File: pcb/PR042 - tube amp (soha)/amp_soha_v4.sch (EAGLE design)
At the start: 55 parts, among them IC1 NE5532, IC2 7812, IC3 7912, Q1 J113, Q2 J113, Q3 J113, Q4 J113

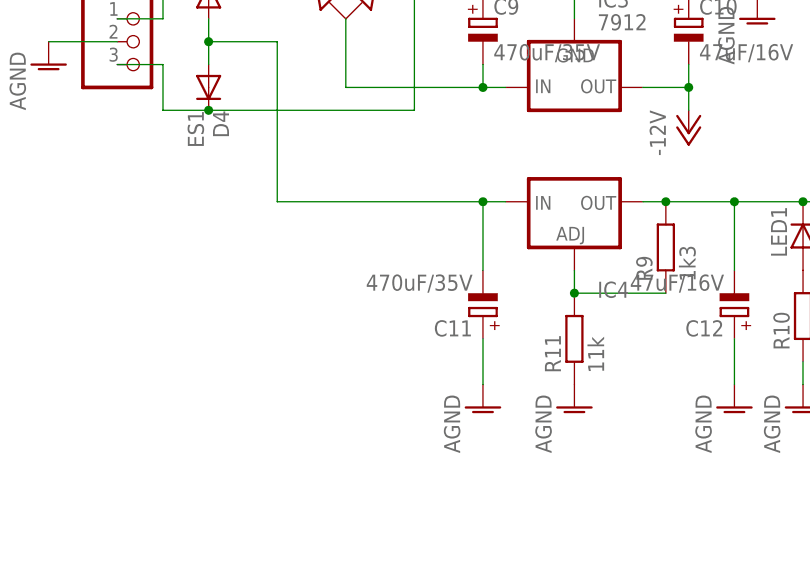
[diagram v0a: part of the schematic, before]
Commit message: 
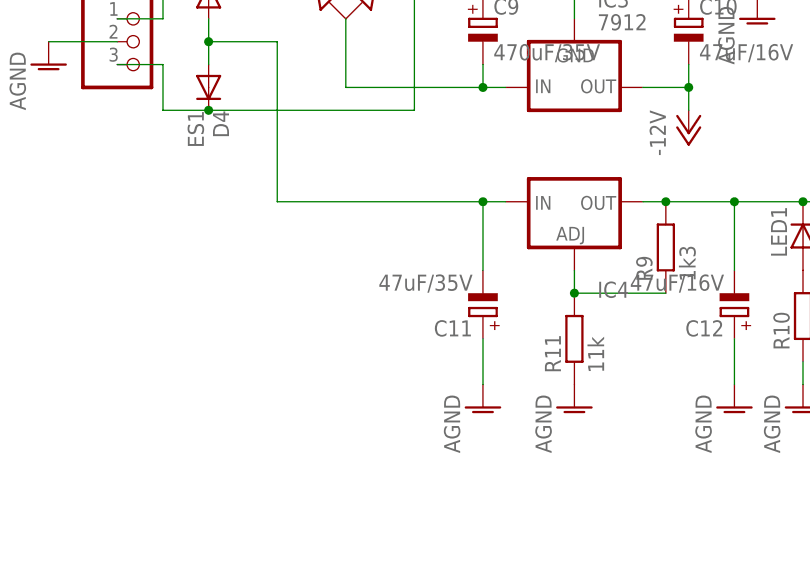
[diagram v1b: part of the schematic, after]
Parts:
- C11: value 470uF/35V -> 47uF/35V; device amp_soha:CPOL-EUE5-10,5 -> amp_soha:CPOL-EUE2.5-6
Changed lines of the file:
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@@
 <part name="AGND1" library="amp_soha" deviceset="AGND" device=""/>
 <part name="D4" library="amp_soha" deviceset="ES1" device=""/>
-<part name="C11" library="amp_soha" deviceset="CPOL-EU" device="E5-10,5" value="470uF/35V"/>
+<part name="C11" library="amp_soha" deviceset="CPOL-EU" device="E2.5-6" value="47uF/35V"/>
 <part name="AGND2" library="amp_soha" deviceset="AGND" device=""/>
 <part name="R9" library="amp_soha" deviceset="R-EU_" device="" value="1k3"/>

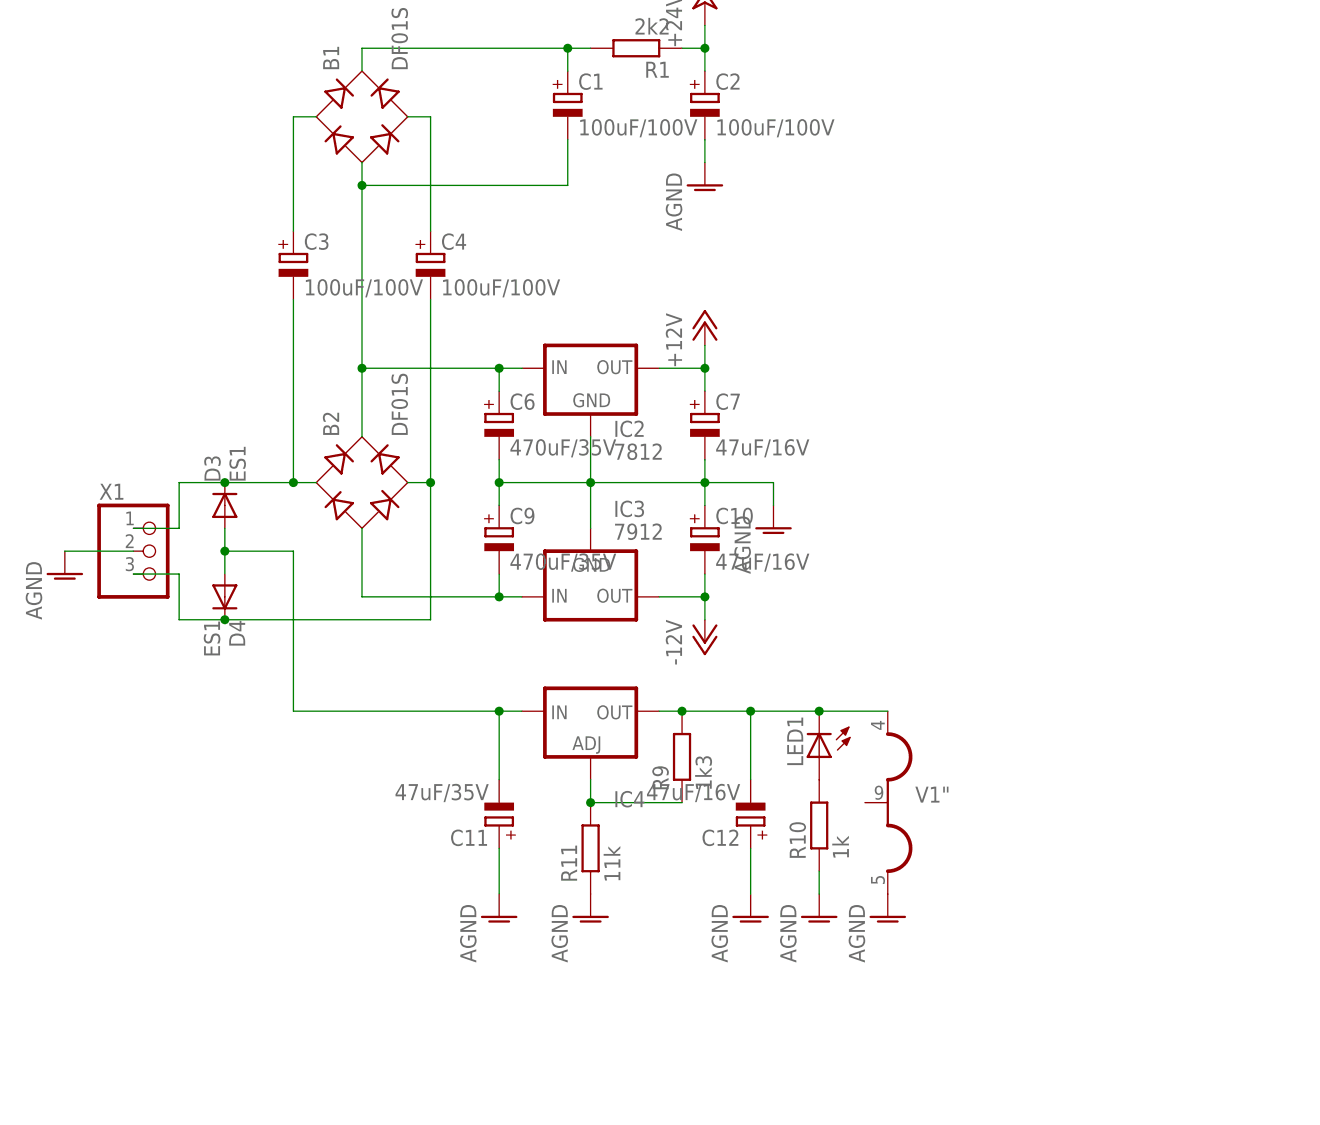
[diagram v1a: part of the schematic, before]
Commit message: 
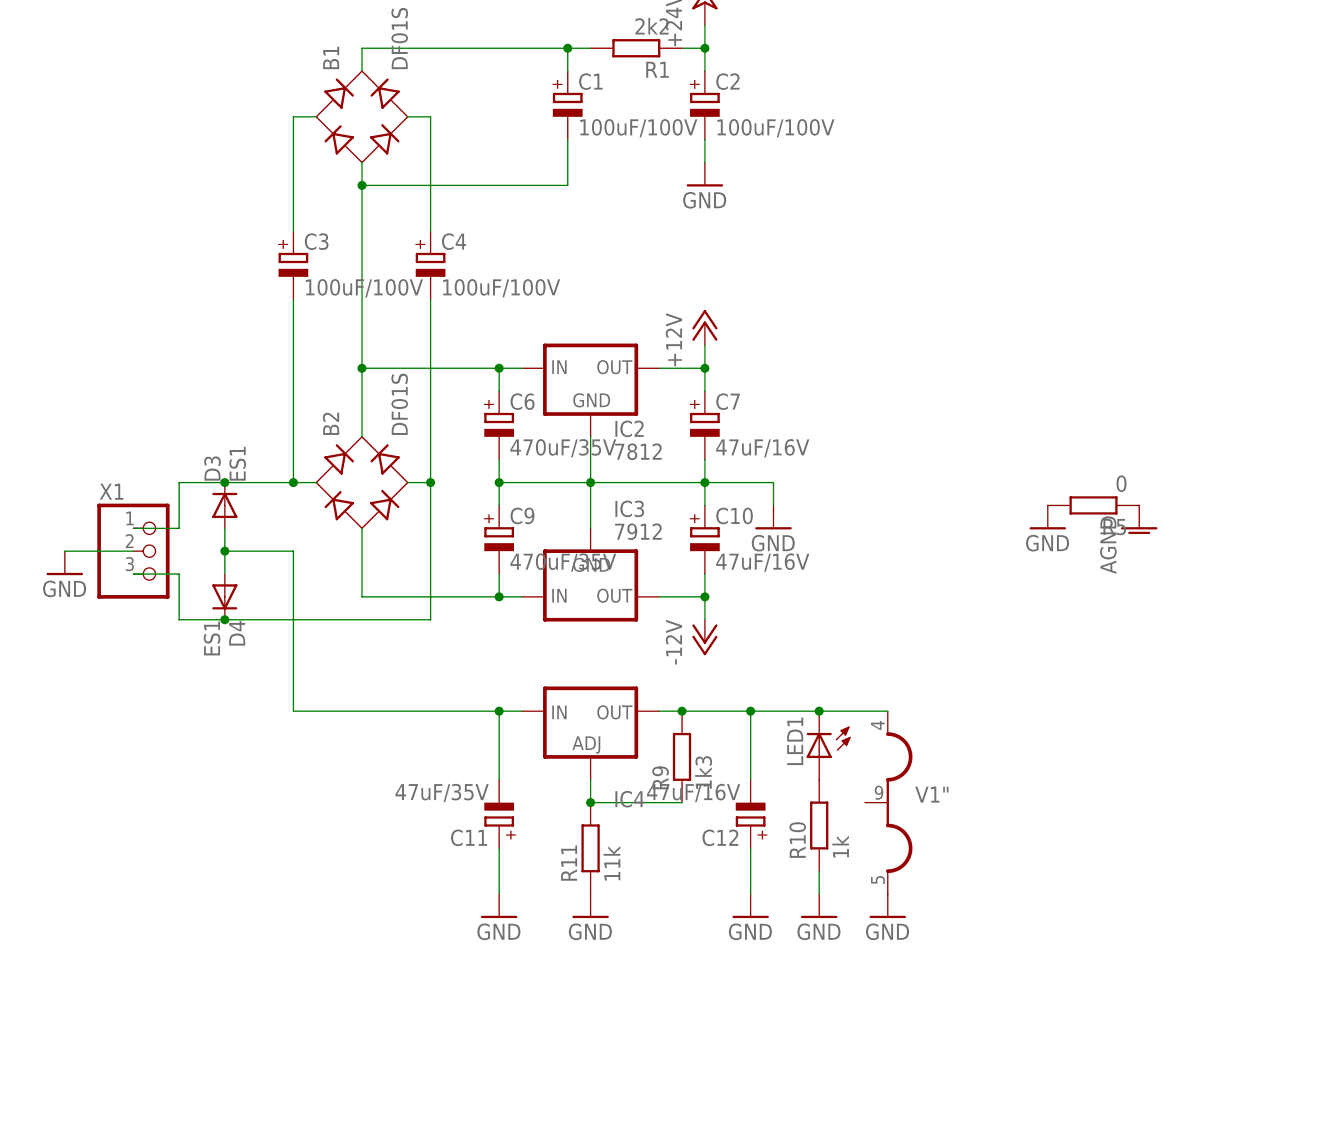
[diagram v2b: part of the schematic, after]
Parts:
- added R5: 0, amp_soha:R-EU_
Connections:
- new net GND: C10.+, C11.+, C12.+, C2.-, C6.-, C7.-, C9.+, IC2.GND, IC3.GND, R10.1, R11.1, R5.2, V1".H3, X1.2
- net AGND: now also R5.1; no longer C10.+, C11.+, C12.+, C2.-, C6.-, C7.-, C9.+, IC2.GND, IC3.GND, R10.1, R11.1, V1".H3, X1.2

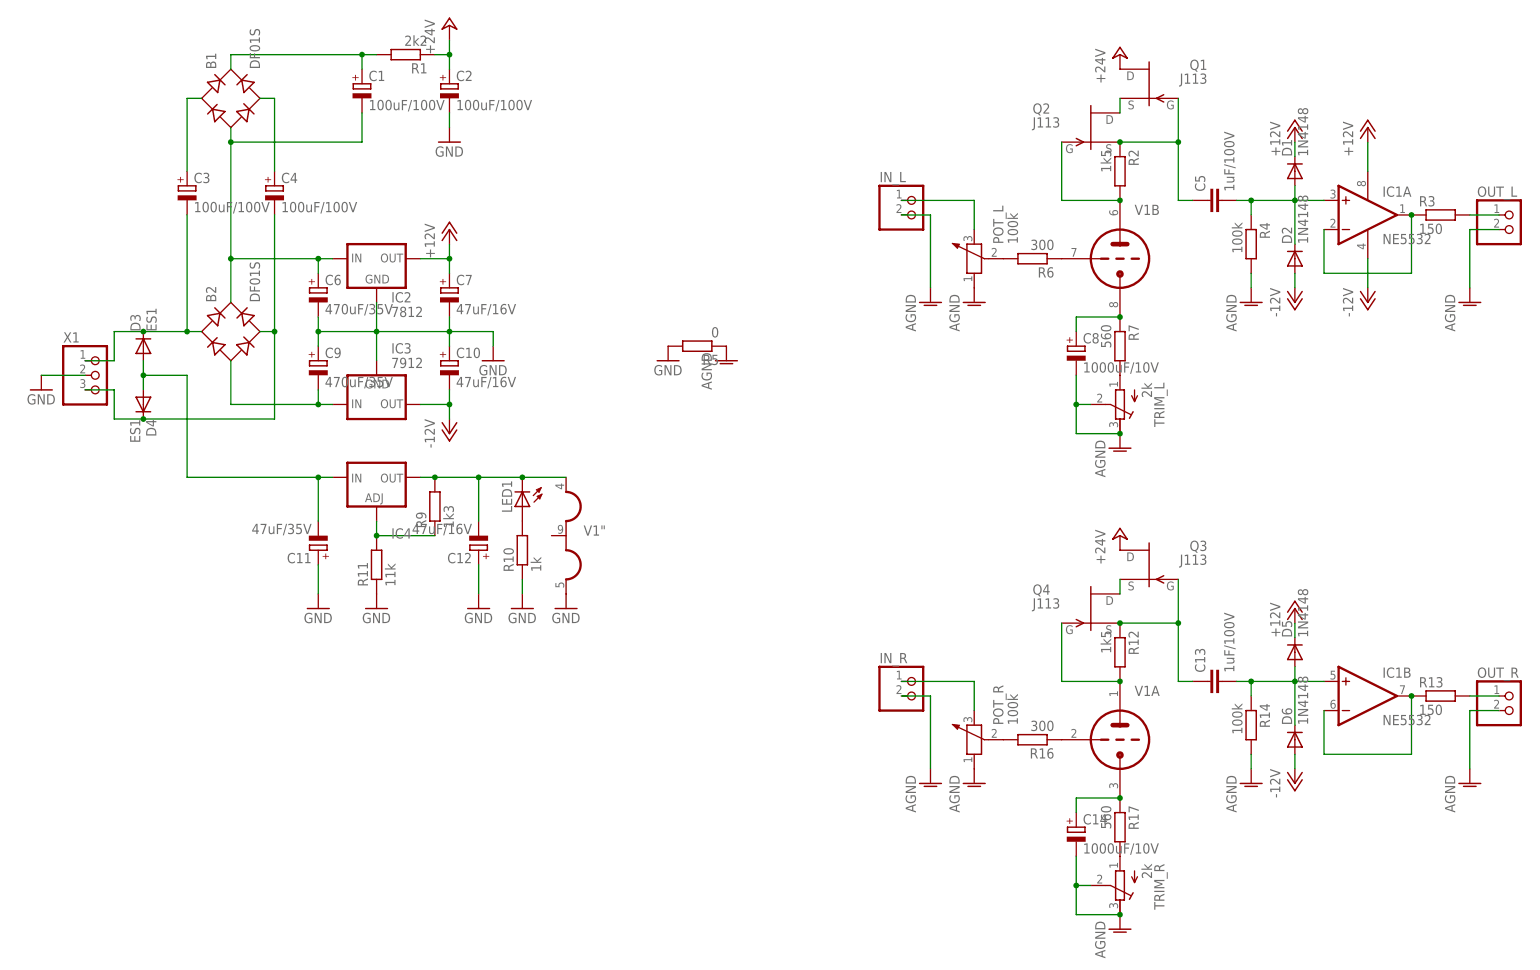
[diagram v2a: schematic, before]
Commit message: 
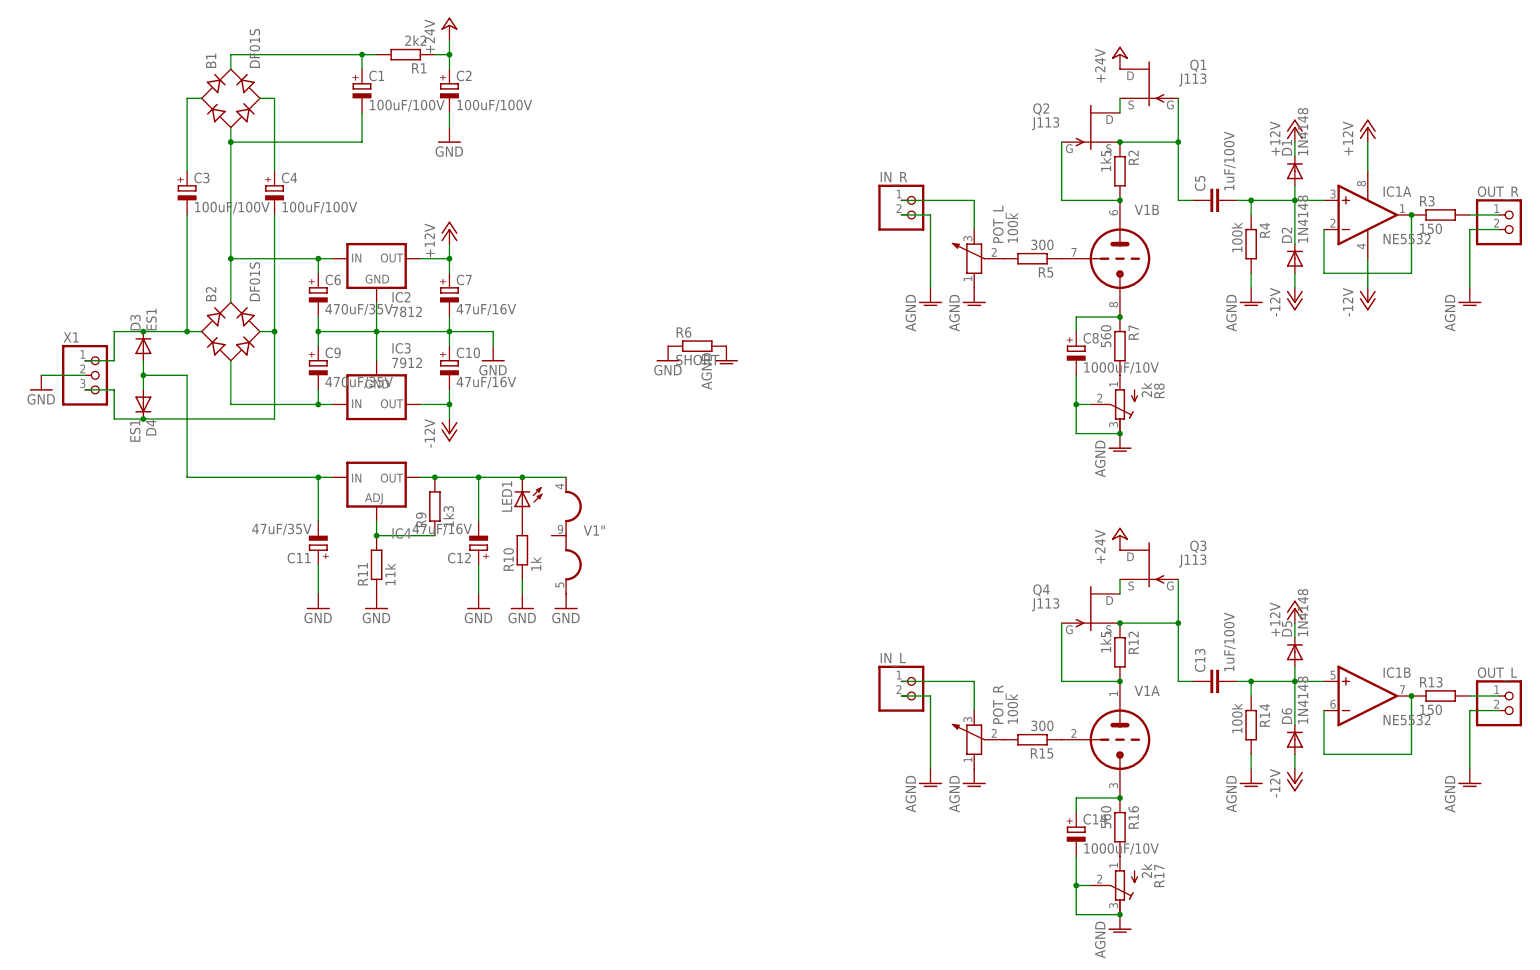
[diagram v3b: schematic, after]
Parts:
- removed TRIM_R: 2k, amp_soha:RTRIM329W
- added R15: 300, amp_soha:R-EU_
- R16: value 300 -> 560
- R17: value 560 -> 2k; device amp_soha:R-EU_ -> amp_soha:RTRIM329W
- R5: value 0 -> 300
- R6: value 300 -> SHORT; device amp_soha:R-EU_ -> amp_soha:SHORT
- renumbered TRIM_L to R8
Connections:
- net AGND: now also R17.E, R17.S, R6.2; no longer R5.1, TRIM_R.E, TRIM_R.S
- net GND: now also R6.1; no longer R5.2
- net N$10: now also R15.1; no longer R16.1
- net N$12: now also IN_R.1; no longer IN_L.1
- net N$13: now also R5.2; no longer R6.2
- net N$14: now also R5.1; no longer R6.1
- net N$18: now also R16.2, R17.A; no longer R17.2, TRIM_R.A
- net N$25: now also OUT_R.1; no longer OUT_L.1
- net N$26: now also IN_L.1; no longer IN_R.1
- net N$27: now also R15.2; no longer R16.2
- net N$29: now also R16.1; no longer R17.1
- net N$36: now also OUT_L.1; no longer OUT_R.1
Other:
- moved on the sheet: IN_L, IN_R, OUT_L, OUT_R, R16, R5, R6
